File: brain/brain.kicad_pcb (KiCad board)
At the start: 2 copper layers, 100 x 80 mm, 180 parts, among them U1 TXB0108, U10 TSR1-2433, U2 74HC154, U3 TXB0108, U4 TXB0108, U5 PCA9306, U6 PCA9685, U7 TXB0108, U8 STM32F407VG, U9 TSR1-2450, Y1 8M

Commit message: Brain 2018 layout
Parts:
- removed AX12, COLOR, STARTER: CONN_3, Sockets_MOLEX_KK-System:Socket_MOLEX-KK-RM2-54mm_Lock_3pin_straight
- removed AX12PWR, PWR: CONN_2, Sockets_MOLEX_KK-System:Socket_MOLEX-KK-RM2-54mm_Lock_2pin_straight
- removed C32, C33: 100n, Capacitors_SMD:C_0603
- removed D1: 1N4148W, Diodes_SMD:SOD-123
- removed ENCL, ENCR, MOTL, MOTR: CONN_5, Sockets_MOLEX_KK-System:Socket_MOLEX-KK-RM2-54mm_Lock_5pin_straight
- removed GYRO, SHIFTREG: CONN_6, Sockets_MOLEX_KK-System:Socket_MOLEX-KK-RM2-54mm_Lock_6pin_straight
- removed I2C5V: CONN_4, Sockets_MOLEX_KK-System:Socket_MOLEX-KK-RM2-54mm_Lock_4pin_straight
- removed JTAG, PWM: HE10-20, espitall:HE10_20D
- removed SLAUART, UART_DBG: CONN_01X05, Sockets_MOLEX_KK-System:Socket_MOLEX-KK-RM2-54mm_Lock_5pin_straight
- added COLOR1: CONN_3, Sockets_MOLEX_KK-System:Socket_MOLEX-KK-RM2-54mm_Lock_3pin_straight, F.Cu at (117.6, 98.8)
- added DCM0: CONN_5, Sockets_MOLEX_KK-System:Socket_MOLEX-KK-RM2-54mm_Lock_5pin_straight, F.Cu at (196.3, 113.9)
- added ENCL1: CONN_5, Sockets_MOLEX_KK-System:Socket_MOLEX-KK-RM2-54mm_Lock_5pin_straight, F.Cu at (184.4, 111.1)
- added ENCR1: CONN_5, Sockets_MOLEX_KK-System:Socket_MOLEX-KK-RM2-54mm_Lock_5pin_straight, F.Cu at (184.4, 118.6)
- added GYRO1: CONN_6, Sockets_MOLEX_KK-System:Socket_MOLEX-KK-RM2-54mm_Lock_6pin_straight, F.Cu at (183.1, 126.1)
- added I2C5V1: CONN_4, Sockets_MOLEX_KK-System:Socket_MOLEX-KK-RM2-54mm_Lock_4pin_straight, F.Cu at (132.6, 62.5)
- added JTAG1: HE10-20, espitall:HE10_20D, F.Cu at (195.1, 88.9)
- added MOTL1: CONN_5, Sockets_MOLEX_KK-System:Socket_MOLEX-KK-RM2-54mm_Lock_5pin_straight, F.Cu at (107.2, 68.1)
- added MOTR1: CONN_5, Sockets_MOLEX_KK-System:Socket_MOLEX-KK-RM2-54mm_Lock_5pin_straight, F.Cu at (107.2, 75.7)
- added PWR1: CONN_2, Sockets_MOLEX_KK-System:Socket_MOLEX-KK-RM2-54mm_Lock_2pin_straight, F.Cu at (104.0, 61.2)
- added R13: 1k, Resistors_SMD:R_0603, F.Cu at (115.4, 104.4)
- added R14: 1k, Resistors_SMD:R_0603, F.Cu at (115.4, 105.9)
- added R16: 1k, Resistors_SMD:R_0603, F.Cu at (123.5, 103.8)
- added R33: 1k, Resistors_SMD:R_0603, F.Cu at (123.5, 105.3)
- added R43: 1k, Resistors_SMD:R_0603, F.Cu at (123.5, 106.9)
- added R44: 1k, Resistors_SMD:R_0603, F.Cu at (112.2, 102.9)
- added R45: 1k, Resistors_SMD:R_0603, B.Cu at (178.6, 106.6)
- added R46: 1k, Resistors_SMD:R_0603, B.Cu at (176.6, 107.4)
- added R9: 1k, Resistors_SMD:R_0603, F.Cu at (115.4, 102.9)
- added SERVO_0-3: CONN_5, Sockets_MOLEX_KK-System:Socket_MOLEX-KK-RM2-54mm_Lock_5pin_straight, F.Cu at (144.7, 53.6)
- added SERVO_4-7: CONN_5, Sockets_MOLEX_KK-System:Socket_MOLEX-KK-RM2-54mm_Lock_5pin_straight, F.Cu at (144.8, 60.7)
- added SERVO_8-13: CONN_5, Sockets_MOLEX_KK-System:Socket_MOLEX-KK-RM2-54mm_Lock_5pin_straight, F.Cu at (148.5, 71.9)
- added SHIFTREG1: CONN_6, Sockets_MOLEX_KK-System:Socket_MOLEX-KK-RM2-54mm_Lock_6pin_straight, F.Cu at (156.9, 69.1)
- added SLAUART1: CONN_01X05, Sockets_MOLEX_KK-System:Socket_MOLEX-KK-RM2-54mm_Lock_5pin_straight, F.Cu at (195.4, 65.5)
- added STARTER1: CONN_3, Sockets_MOLEX_KK-System:Socket_MOLEX-KK-RM2-54mm_Lock_3pin_straight, F.Cu at (117.6, 91.0)
- added UART_DBG1: CONN_01X05, Sockets_MOLEX_KK-System:Socket_MOLEX-KK-RM2-54mm_Lock_5pin_straight, F.Cu at (159.0, 98.4)
- BOOT0, BOOT1: footprint Pin_Headers:Pin_Header_Straight_1x02 -> Pin_Headers:Pin_Header_Straight_1x02_Pitch2.54mm
- C2: value 100n -> 4u7; moved to B.Cu
- R15: moved to F.Cu
- U1, U3: value TXB0108 -> SN74AHCT125PW; footprint Housings_SSOP:TSSOP-20_4.4x6.5mm_Pitch0.65mm -> Housings_SSOP:TSSOP-14_4.4x5mm_Pitch0.65mm
- U4: value TXB0108 -> SN74AHCT125PW; footprint Housings_SSOP:TSSOP-20_4.4x6.5mm_Pitch0.65mm -> Housings_SSOP:TSSOP-14_4.4x5mm_Pitch0.65mm; moved to B.Cu
- moved R15 80.0 mm to (112.8, 107.2), turned to 180 degrees
- moved C2 71.0 mm to (188.8, 107.6), turned to 180 degrees
- moved U4 67.0 mm to (175.0, 117.3), turned to 270 degrees
- moved C27 16.5 mm to (173.8, 121.9)
- moved C28 6.51 mm to (173.3, 107.6)
- moved C30 6.38 mm to (193.1, 118.4), turned to 90 degrees
- moved C1 5.78 mm to (116.3, 109.2), turned to 0 degrees
- moved U3 1.71 mm to (172.1, 104.6), turned to 270 degrees
- moved U1 0.46 mm to (117.5, 104.9), turned to 270 degrees
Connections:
- C2 pad 1: +3V3 -> +5V
- C27 pad 1: +3V3 -> +5V
- H1 pad 1: GND -> (no net)
- H2 pad 1: GND -> (no net)
- H3 pad 1: GND -> (no net)
- H4 pad 1: GND -> (no net)
- R15 pad 1: +5V -> /USIR/US_CH3_E_3v3
- R15 pad 2: Net-(AX12-Pad1) -> /USIR/US_CH3_E_5v
- U1 pad 1: /USIR/US_CH0_T_3v3 -> GND
- U1 pad 10: +3V3 -> GND
- U1 pad 11: GND -> /USIR/US_CH3_T_5v
- U1 pad 12: /USIR/US_CH3_E_5v -> /USIR/US_CH3_T_3v3
- U1 pad 13: /USIR/US_CH3_T_5v -> GND
- U1 pad 14: /USIR/US_CH2_E_5v -> +5V
- U1 pad 2: +3V3 -> /USIR/US_CH0_T_3v3
- U1 pad 3: /USIR/US_CH0_E_3v3 -> /USIR/US_CH0_T_5v
- U1 pad 4: /USIR/US_CH1_T_3v3 -> GND
- U1 pad 5: /USIR/US_CH1_E_3v3 -> /USIR/US_CH1_T_3v3
- U1 pad 6: /USIR/US_CH2_T_3v3 -> /USIR/US_CH1_T_5v
- U1 pad 7: /USIR/US_CH2_E_3v3 -> GND
- U1 pad 8: /USIR/US_CH3_T_3v3 -> /USIR/US_CH2_T_5v
- U1 pad 9: /USIR/US_CH3_E_3v3 -> /USIR/US_CH2_T_3v3
- U2 pad 1: Net-(U2-Pad1) -> (no net)
- U2 pad 15: Net-(U2-Pad15) -> (no net)
- U2 pad 16: Net-(U2-Pad16) -> (no net)
- U2 pad 17: Net-(U2-Pad17) -> (no net)
- U3 pad 1: /Position/POS_SPI_CSL_3v3 -> GND
- U3 pad 10: +3V3 -> GND
- U3 pad 11: GND -> /Position/POS_SPI_MOSI_5v
- U3 pad 12: /Position/AX12_RX_5v -> /Position/POS_SPI_MOSI_3v3
- U3 pad 13: /Position/AX12_RX_5v -> GND
- U3 pad 14: /Position/POS_SPI_MOSI_5v -> +5V
- U3 pad 2: +3V3 -> /Position/POS_SPI_CSL_3v3
- U3 pad 3: /Position/POS_SPI_CSR_3v3 -> /Position/POS_SPI_CSL_5v
- U3 pad 4: /Position/POS_SPI_CSG_3v3 -> GND
- U3 pad 5: /Position/POS_SPI_SCK_3v3 -> /Position/POS_SPI_CSR_3v3
- U3 pad 6: /Position/POS_SPI_MISO_3v3 -> /Position/POS_SPI_CSR_5v
- U3 pad 7: /Position/POS_SPI_MOSI_3v3 -> GND
- U3 pad 8: /Position/AX12_TX_3v3 -> /Position/POS_SPI_SCK_5v
- U3 pad 9: /Position/AX12_RX_3v3 -> /Position/POS_SPI_SCK_3v3
- U4 pad 1: /Position/MOT_ENA_3v3 -> GND
- U4 pad 10: +3V3 -> GND
- U4 pad 11: GND -> (no net)
- U4 pad 12: GND -> (no net)
- U4 pad 14: GND -> +5V
- U4 pad 2: +3V3 -> /Position/POS_SPI_CSG_3v3
- U4 pad 3: /Position/MOTL_DIR_3v3 -> /Position/POS_SPI_CSG_5v
- U4 pad 4: /Position/MOTR_DIR_3v3 -> GND
- U4 pad 5: /Position/MOTL_PWM_3v3 -> (no net)
- U4 pad 6: /Position/MOTR_PWM_3v3 -> (no net)
- U4 pad 7: Net-(U4-Pad7) -> GND
- U4 pad 8: Net-(U4-Pad8) -> (no net)
- U4 pad 9: Net-(U4-Pad9) -> (no net)
- U6 pad 19: Net-(PWM1-Pad8) -> (no net)
- U6 pad 20: Net-(PWM1-Pad6) -> (no net)
- U6 pad 21: Net-(PWM1-Pad4) -> (no net)
- U6 pad 22: Net-(PWM1-Pad2) -> (no net)
- U8 pad 1: /Position/MOT_ENA_3v3 -> /DC motor/MOT_ENA_3v3
- U8 pad 15: Net-(U8-Pad15) -> (no net)
- U8 pad 18: Net-(U8-Pad18) -> (no net)
- U8 pad 34: Net-(U8-Pad34) -> (no net)
- U8 pad 47: /Position/AX12_TX_3v3 -> /DC motor/DCM0_PWM_3v3
- U8 pad 48: /Position/AX12_RX_3v3 -> (no net)
- U8 pad 58: Net-(U8-Pad58) -> (no net)
- U8 pad 62: Net-(U8-Pad62) -> (no net)
- U8 pad 64: Net-(U8-Pad64) -> (no net)
- U8 pad 67: Net-(U8-Pad67) -> /DC motor/DCM0_DIR_3v3
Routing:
- net /DC motor/MOT_ENA_3v3: track 0.00 -> 223.1 mm, vias 0 -> 2
- net /DC motor/DCM0_DIR_3v3: track 0.00 -> 72.7 mm, vias 0 -> 4
- net /DC motor/DCM0_PWM_3v3: track 0.00 -> 68.6 mm, vias 0 -> 2
- net GND: track 1283.3 -> 1325.1 mm, vias 31 -> 41
- net +3V3: track 653.4 -> 613.1 mm, vias 31 -> 28
- net /Position/MOT_ENA_3v3: track 29.6 -> 0.00 mm
- net Net-(PWM1-Pad2): track 27.8 -> 0.00 mm
- net /Position/AX12_TX_3v3: track 24.0 -> 0.00 mm
- net /Position/AX12_RX_3v3: track 22.8 -> 0.00 mm
- net /Position/MOTL_PWM_3v3: track 26.6 -> 48.7 mm, vias 0 -> 2
- net /Position/MOTL_DIR_5v: track 22.1 -> 0.00 mm
- net /Position/MOTL_DIR_3v3: track 28.3 -> 50.0 mm
- net /Position/MOT_ENA_5v: track 21.4 -> 0.00 mm
- net Net-(PWM1-Pad4): track 21.4 -> 0.00 mm
- net /Position/MOTL_PWM_5v: track 20.7 -> 0.00 mm
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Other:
- board text added: "Brain Eurobot 2018 Cocobot"
- board text removed: "Brain Eurobot 2016 ~espitall"

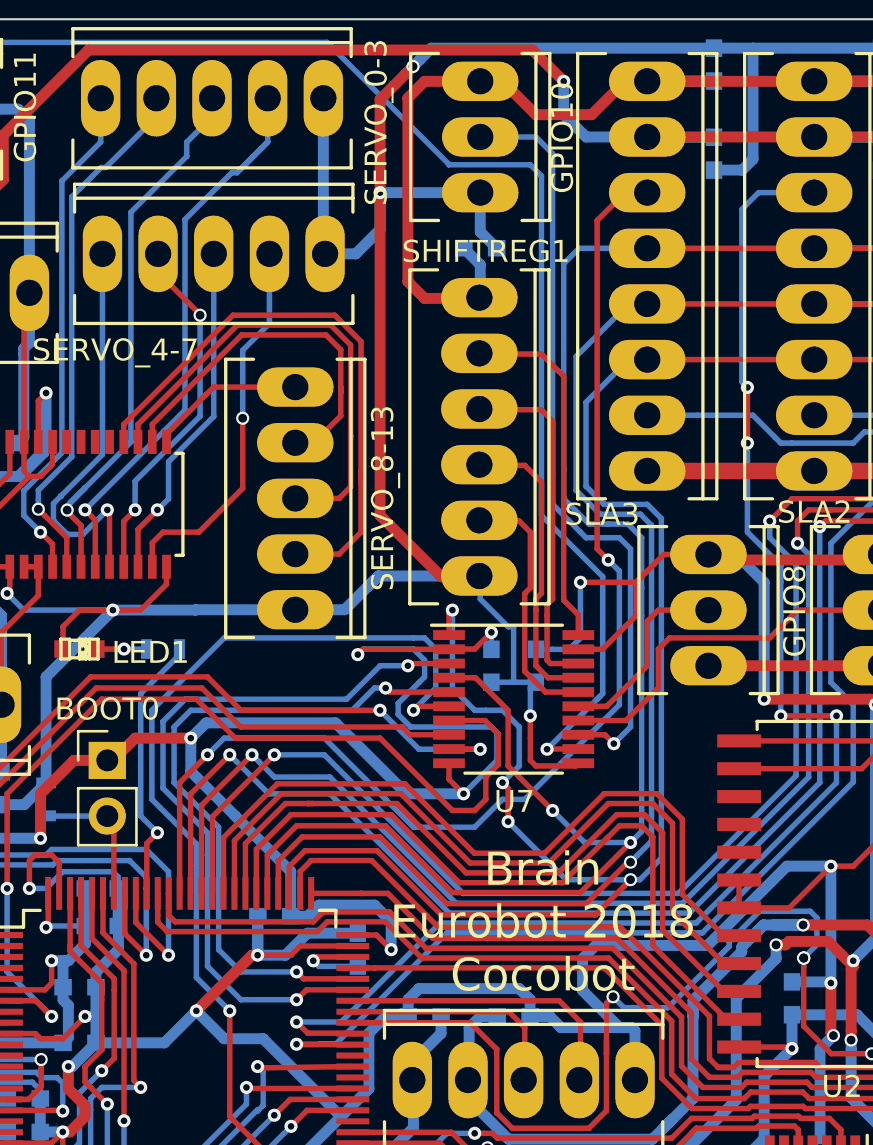
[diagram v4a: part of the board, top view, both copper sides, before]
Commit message: change shift register connector to match Cocoout and Cocoin
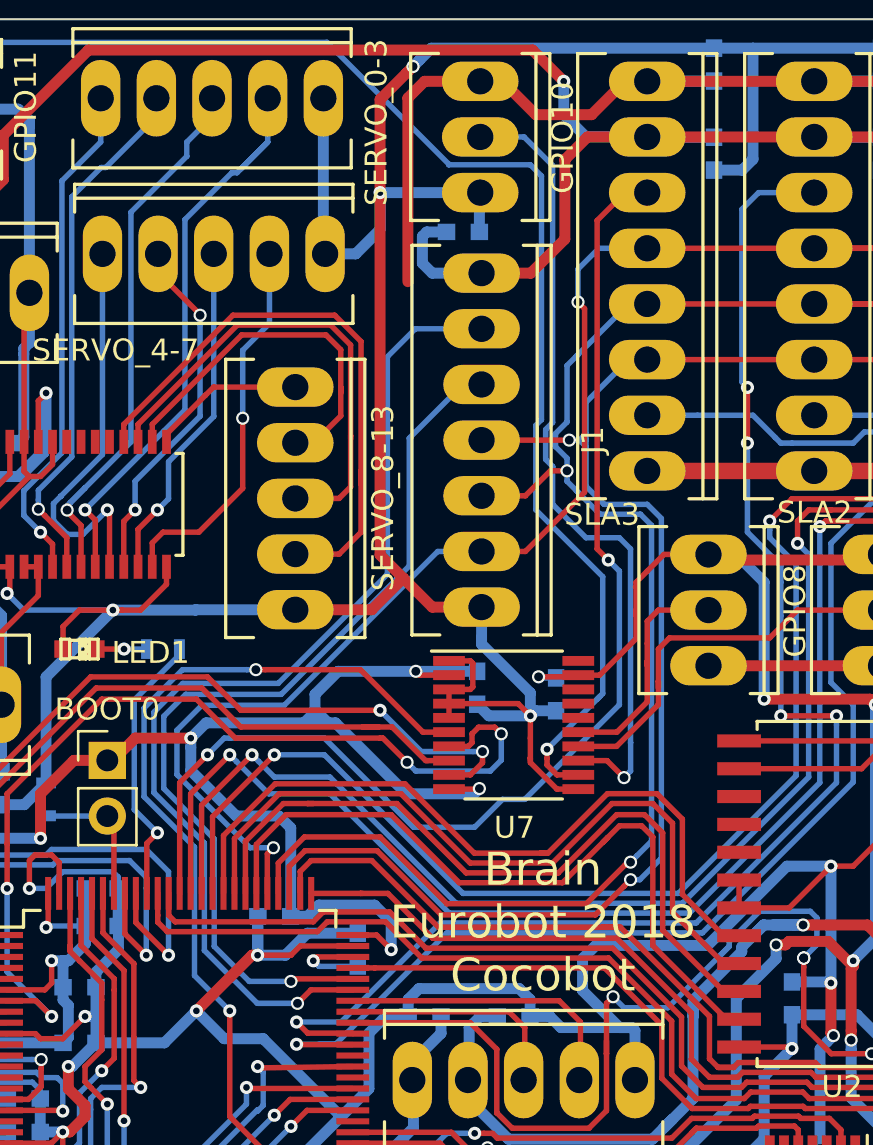
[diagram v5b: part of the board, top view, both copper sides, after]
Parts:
- removed SHIFTREG1: CONN_6, Sockets_MOLEX_KK-System:Socket_MOLEX-KK-RM2-54mm_Lock_6pin_straight
- added J1: CONN_01X07, espitall:Socket_MOLEX-KK-RM2-54mm_Lock_7pin_straight, F.Cu at (157.0, 69.2)
- moved C58 1.60 mm to (160.4, 80.8)
- moved C57 1.19 mm to (156.8, 80.5)
- moved U7 1.18 mm to (158.5, 82.2)
- moved C61 1.09 mm to (156.2, 59.7)
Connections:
- net /Slave/SLA_SPI_MISO_3v3 renamed /GPIO/SLA_SPI_MISO_3v3
- C61 pad 1: +5V -> +3V3
- U7 pad 1: /GPIO/SLA_SPI_SCK_3v3 -> GND
- U7 pad 16: /GPIO/GPIO_SHIFT_OE_5V -> (no net)
- U7 pad 17: /GPIO/GPIO_SHIFT_DATA_5V -> (no net)
- U7 pad 18: /GPIO/GPIO_SHIFT_STCP_5V -> (no net)
- U7 pad 20: /GPIO/GPIO_SHIFT_SHCP_5V -> (no net)
- U7 pad 3: /GPIO/GPIO_SHIFT_STCP_3v3 -> GND
- U7 pad 4: /GPIO/SLA_SPI_MOSI_3v3 -> GND
- U7 pad 5: /GPIO/GPIO_SHIFT_OE_3v3 -> GND
- U8 pad 70: /GPIO/GPIO_SHIFT_STCP_3v3 -> /GPIO/GPIO_SHIFT_LOAD_3v3
- U8 pad 71: /GPIO/GPIO_SHIFT_OE_3v3 -> /GPIO/GPIO_SHIFT_SET_3v3
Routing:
- net /GPIO/GPIO_SHIFT_LOAD_3v3: track 0.00 -> 47.9 mm, vias 0 -> 1
- net /GPIO/GPIO_SHIFT_SET_3v3: track 0.00 -> 42.7 mm, vias 0 -> 1
- net /GPIO/GPIO_SHIFT_STCP_3v3: track 33.6 -> 0.00 mm, vias 2 -> 0
- net /GPIO/GPIO_SHIFT_OE_3v3: track 31.0 -> 0.00 mm, vias 2 -> 0
- net /GPIO/SLA_SPI_MOSI_3v3: track 150.8 -> 130.5 mm
- net /GPIO/GPIO_SHIFT_SHCP_5V: track 16.3 -> 0.00 mm
- net /GPIO/GPIO_SHIFT_STCP_5V: track 16.0 -> 0.00 mm
- net /GPIO/SLA_SPI_SCK_3v3: track 124.5 -> 110.2 mm, vias 4 -> 2
- net /GPIO/GPIO_SHIFT_DATA_5V: track 13.8 -> 0.00 mm
- net /GPIO/GPIO_SHIFT_OE_5V: track 11.8 -> 0.00 mm
- net +3V3: track 613.1 -> 622.8 mm, vias 28 -> 27
- net +5V: track 693.4 -> 683.9 mm
- net GND: track 1325.1 -> 1331.5 mm
- net /GPIO/SLA_SPI_MISO_3v3: track 128.4 -> 134.0 mm, vias 1 -> 2
- net /GPIO/GPIO8_3v3: track 45.8 -> 42.4 mm
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
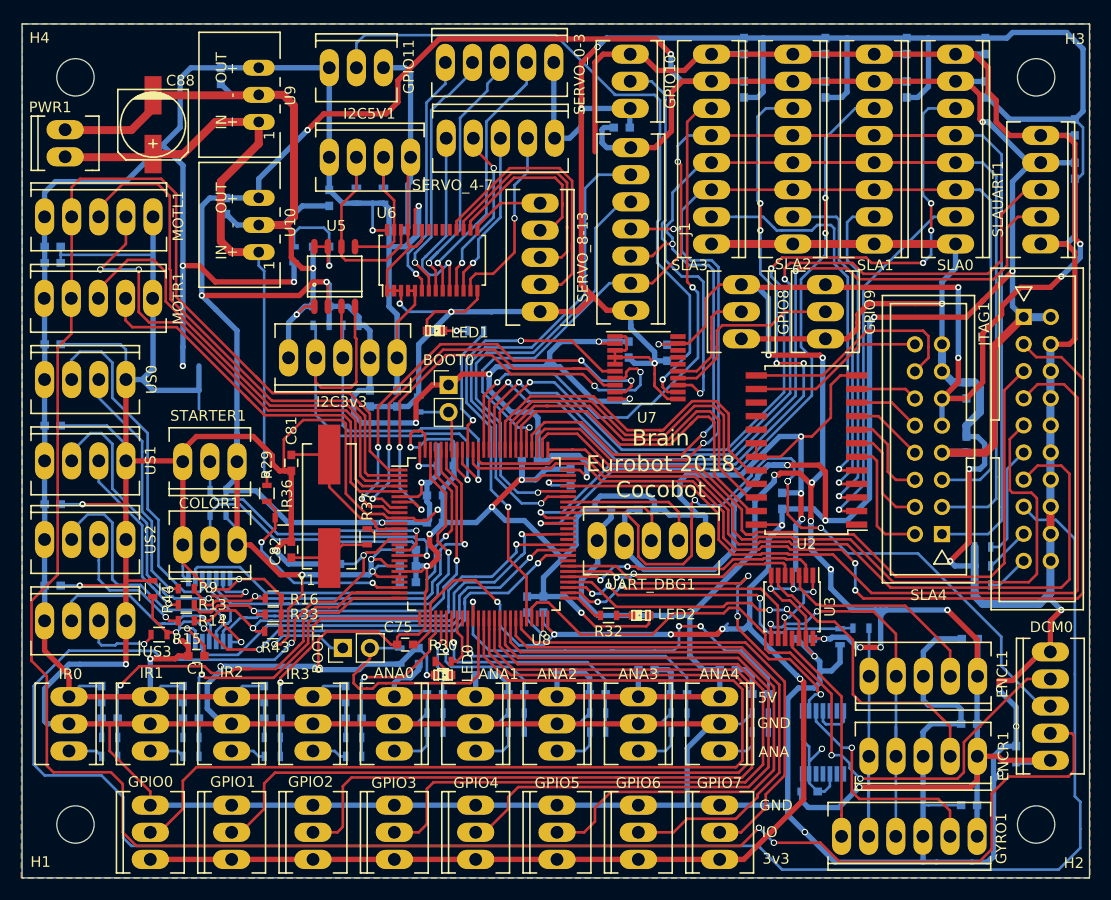
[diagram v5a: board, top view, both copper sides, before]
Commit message: add 3d step files to brain
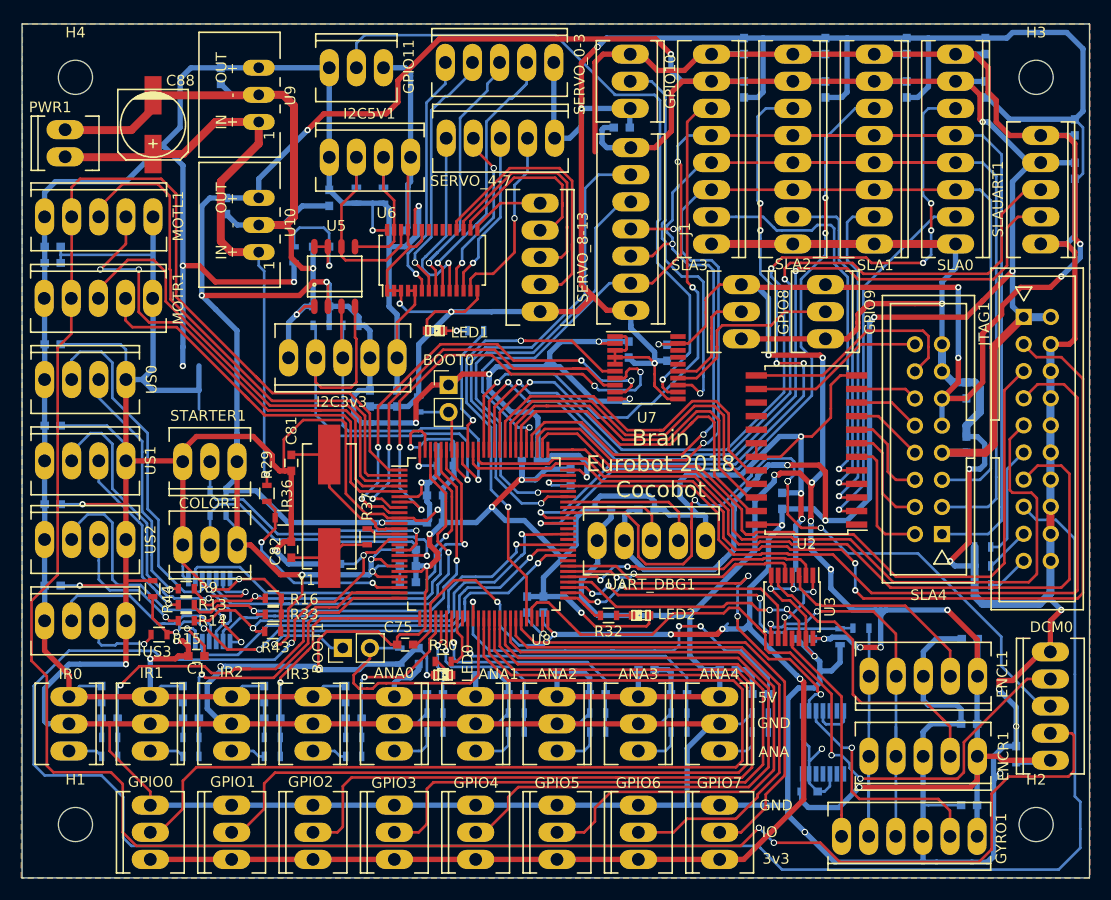
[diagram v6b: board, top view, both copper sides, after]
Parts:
- ANA0, ANA1, ANA2, ANA3, ANA4, COLOR1, GPIO0, GPIO1, GPIO10, GPIO11, GPIO2, GPIO3, GPIO4, GPIO5, GPIO6, GPIO7, GPIO8, GPIO9, IR0, IR1, IR2, IR3, STARTER1: footprint Sockets_MOLEX_KK-System:Socket_MOLEX-KK-RM2-54mm_Lock_3pin_straight -> espitall:Socket_MOLEX-KK-RM2-54mm_Lock_3pin_straight
- BOOT0, BOOT1: footprint Pin_Headers:Pin_Header_Straight_1x02_Pitch2.54mm -> espitall:Pin_Header_Straight_1x02_Pitch2.54mm
- C1, C10, C11, C12, C13, C14, C15, C16, C17, C18, C19, C2, C20, C21, C22, C23, C24, C25, C26, C27, C28, C29, C3, C30, C31, C34, C39, C4, C40, C41, C46, C47, C5, C52, C57, C58, C59, C6, C60, C61, C62, C63, C64, C65, C66, C67, C68, C69, C7, C70, C71, C72, C73, C74, C75, C76, C77, C78, C79, C8, C80, C81, C82, C83, C84, C85, C86, C87, C89, C9, C90, C91: footprint Capacitors_SMD:C_0603 -> espitall:C_0603
- C88: footprint Capacitors_SMD:c_elec_6.3x7.7 -> espitall:c_elec_6.3x7.7
- DCM0, ENCL1, ENCR1, I2C3v3, MOTL1, MOTR1, SERVO_0-3, SERVO_4-7, SERVO_8-13, SLAUART1, UART_DBG1: footprint Sockets_MOLEX_KK-System:Socket_MOLEX-KK-RM2-54mm_Lock_5pin_straight -> espitall:Socket_MOLEX-KK-RM2-54mm_Lock_5pin_straight
- GYRO1: footprint Sockets_MOLEX_KK-System:Socket_MOLEX-KK-RM2-54mm_Lock_6pin_straight -> espitall:Socket_MOLEX-KK-RM2-54mm_Lock_6pin_straight
- H1, H2, H3, H4: footprint Mounting_Holes:MountingHole_3-5mm -> Mounting_Holes:MountingHole_3.2mm_M3
- I2C5V1, US0, US1, US2, US3: footprint Sockets_MOLEX_KK-System:Socket_MOLEX-KK-RM2-54mm_Lock_4pin_straight -> espitall:Socket_MOLEX-KK-RM2-54mm_Lock_4pin_straight
- LED0, LED1, LED2: footprint LEDs:LED-0603 -> espitall:LED-0603
- PWR1: footprint Sockets_MOLEX_KK-System:Socket_MOLEX-KK-RM2-54mm_Lock_2pin_straight -> espitall:Socket_MOLEX-KK-RM2-54mm_Lock_2pin_straight
- R1, R10, R11, R12, R13, R14, R15, R16, R17, R18, R19, R2, R20, R21, R22, R23, R24, R25, R26, R27, R28, R29, R3, R30, R31, R32, R33, R34, R35, R36, R37, R38, R39, R4, R40, R41, R42, R43, R44, R45, R46, R5, R6, R7, R8, R9: footprint Resistors_SMD:R_0603 -> espitall:R_0603
- U1, U3, U4: footprint Housings_SSOP:TSSOP-14_4.4x5mm_Pitch0.65mm -> espitall:TSSOP-14_4.4x5mm_Pitch0.65mm
- U2: footprint Housings_SOIC:SOIC-24_7.5x15.4mm_Pitch1.27mm -> espitall:SOIC-24_7.5x15.4mm_Pitch1.27mm
- U5: footprint Power_Integrations:SO-8 -> espitall:SO-8
- U6: footprint Housings_SSOP:TSSOP-28_4.4x9.7mm_Pitch0.65mm -> espitall:TSSOP-28_4.4x9.7mm_Pitch0.65mm
- U7: footprint Housings_SSOP:TSSOP-20_4.4x6.5mm_Pitch0.65mm -> espitall:TSSOP-20_4.4x6.5mm_Pitch0.65mm
- U8: footprint Housings_QFP:LQFP-100_14x14mm_Pitch0.5mm -> espitall:LQFP-100_14x14mm_Pitch0.5mm
- Y1: footprint Crystals:Crystal_HC49-SD_SMD -> espitall:Crystal_HC49-SD_SMD
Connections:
- H1 pad 1: (no net) -> Net-(H1-Pad1)
- H2 pad 1: (no net) -> Net-(H2-Pad1)
- H3 pad 1: (no net) -> Net-(H3-Pad1)
- H4 pad 1: (no net) -> Net-(H4-Pad1)
- U2 pad 1: (no net) -> Net-(U2-Pad1)
- U2 pad 15: (no net) -> Net-(U2-Pad15)
- U2 pad 16: (no net) -> Net-(U2-Pad16)
- U2 pad 17: (no net) -> Net-(U2-Pad17)
- U4 pad 11: (no net) -> Net-(U4-Pad11)
- U4 pad 12: (no net) -> Net-(U4-Pad12)
- U4 pad 5: (no net) -> Net-(U4-Pad5)
- U4 pad 6: (no net) -> Net-(U4-Pad6)
- U4 pad 8: (no net) -> Net-(U4-Pad8)
- U4 pad 9: (no net) -> Net-(U4-Pad9)
- U6 pad 19: (no net) -> Net-(U6-Pad19)
- U6 pad 20: (no net) -> Net-(U6-Pad20)
- U6 pad 21: (no net) -> Net-(U6-Pad21)
- U6 pad 22: (no net) -> Net-(U6-Pad22)
- U7 pad 16: (no net) -> Net-(U7-Pad16)
- U7 pad 17: (no net) -> Net-(U7-Pad17)
- U7 pad 18: (no net) -> Net-(U7-Pad18)
- U7 pad 20: (no net) -> Net-(U7-Pad20)
- U8 pad 15: (no net) -> Net-(U8-Pad15)
- U8 pad 18: (no net) -> Net-(U8-Pad18)
- U8 pad 34: (no net) -> Net-(U8-Pad34)
- U8 pad 48: (no net) -> /DC motor/DCM1_PWM_3v3
- U8 pad 58: (no net) -> Net-(U8-Pad58)
- U8 pad 62: (no net) -> Net-(U8-Pad62)
- U8 pad 64: (no net) -> /DC motor/DCM1_DIR_3v3
